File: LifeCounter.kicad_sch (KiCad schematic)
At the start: 22 parts, among them U1 MAX7221xWG, U2 CC56-12GWA, U3 CC56-12GWA, U4 74HC595

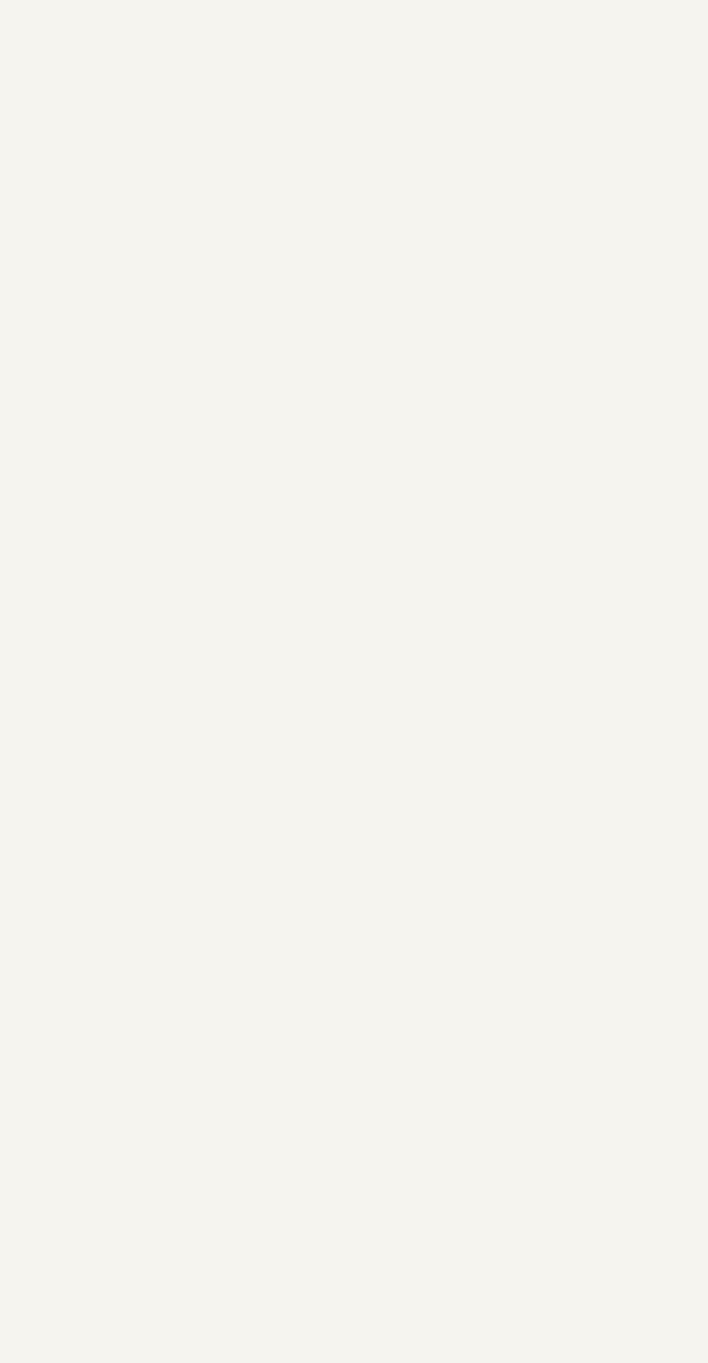
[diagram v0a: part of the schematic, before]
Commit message: Add encoders
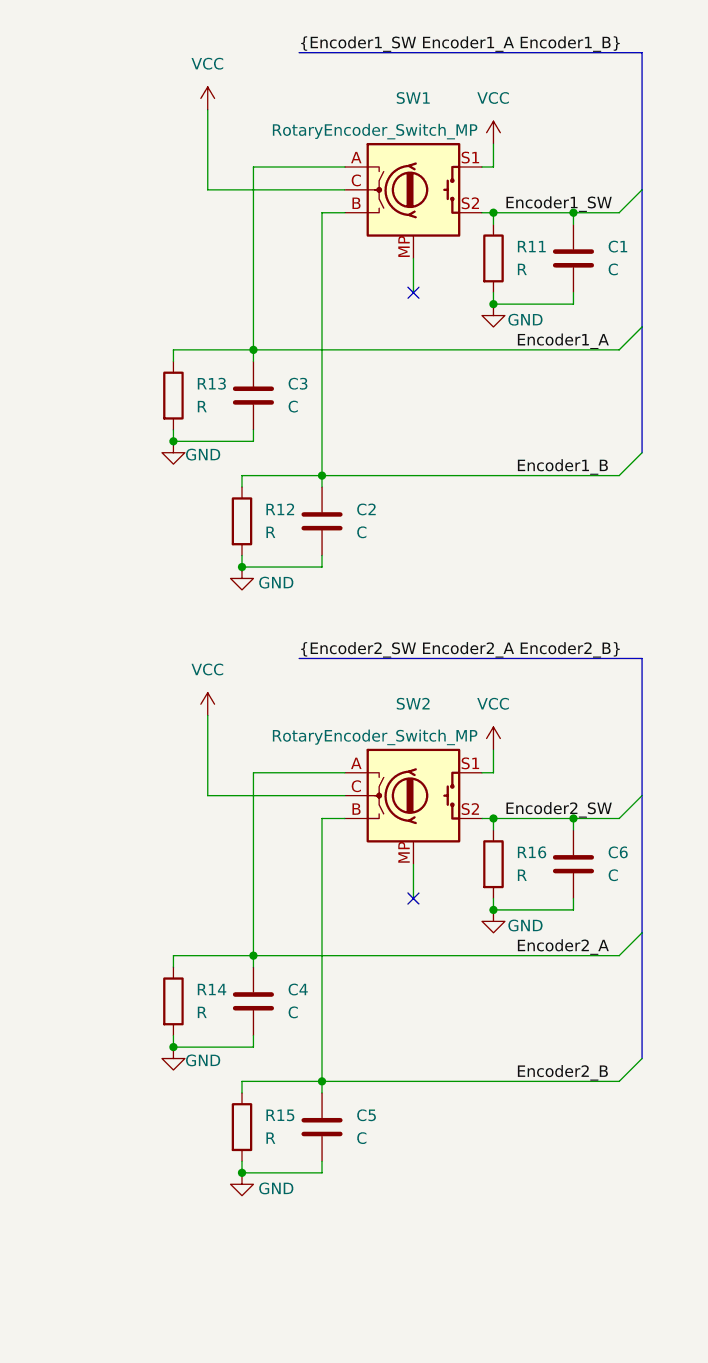
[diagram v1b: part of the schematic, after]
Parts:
- added C1, C2, C3, C4, C5, C6: C, symbol Device:C
- added R11, R12, R13, R14, R15, R16: R, symbol Device:R
- added SW1, SW2: RotaryEncoder_Switch_MP, symbol Device:RotaryEncoder_Switch_MP
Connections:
- net GND: now also C1.2, C2.2, C3.2, C4.2, C5.2, C6.2, R11.2, R12.2, R13.2, R14.2, R15.2, R16.2
- net VCC: now also SW1.C, SW1.S1, SW2.C, SW2.S1
- new net Encoder1_A: C3.1, R13.1, SW1.A
- new net Encoder1_B: C2.1, R12.1, SW1.B
- new net Encoder1_SW: C1.1, R11.1, SW1.S2
- new net Encoder2_A: C4.1, R14.1, SW2.A
- new net Encoder2_B: C5.1, R15.1, SW2.B
- new net Encoder2_SW: C6.1, R16.1, SW2.S2
- no-connect marks 2 -> 4

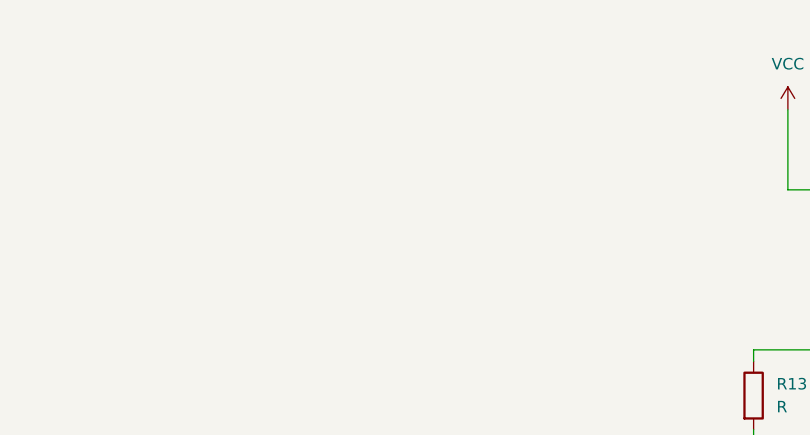
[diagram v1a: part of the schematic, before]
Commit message: Add buzzer
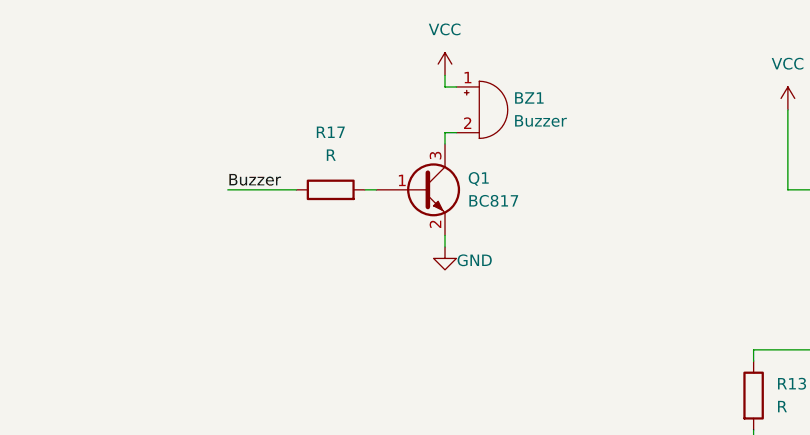
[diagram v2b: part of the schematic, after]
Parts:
- added BZ1: Buzzer, symbol Device:Buzzer
- added Q1: BC817, Package_TO_SOT_SMD:SOT-23, symbol Transistor_BJT:BC817
- added R17: R, symbol Device:R
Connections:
- net GND: now also Q1.2 (E)
- net VCC: now also BZ1.1 (+)
- new net: BZ1.2 (-), Q1.3 (C)
- new net: Q1.1 (B), R17.2
- new net Buzzer: R17.1

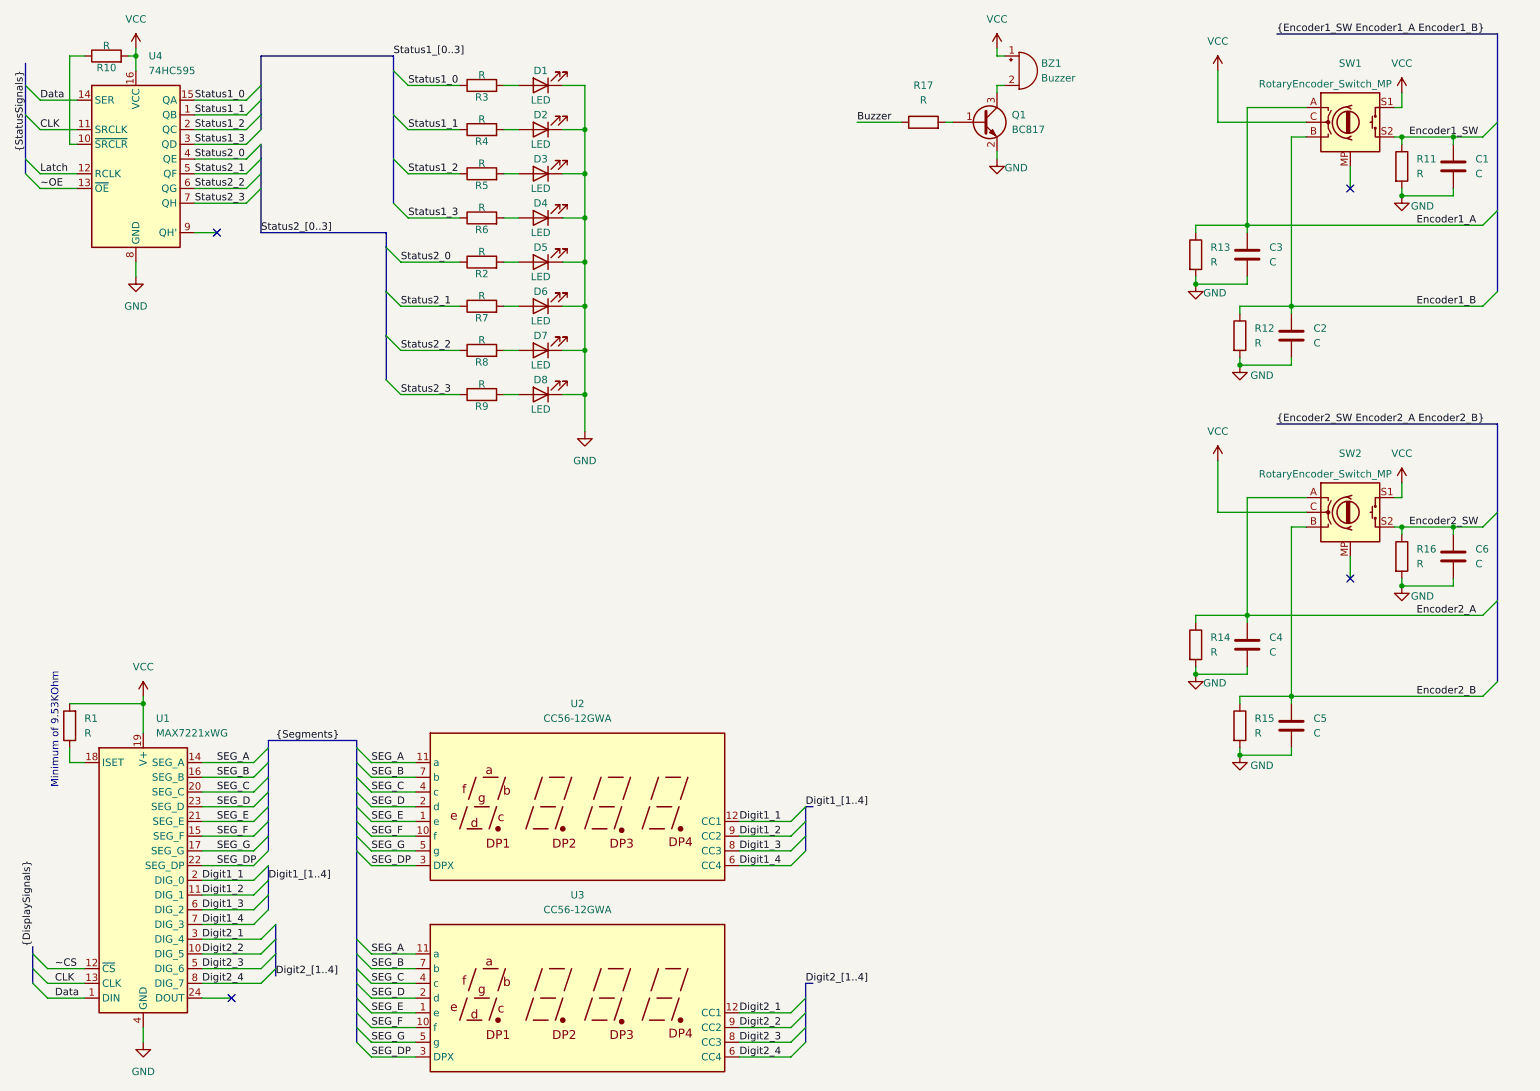
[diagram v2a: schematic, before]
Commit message: Split schematic into multiple sheets
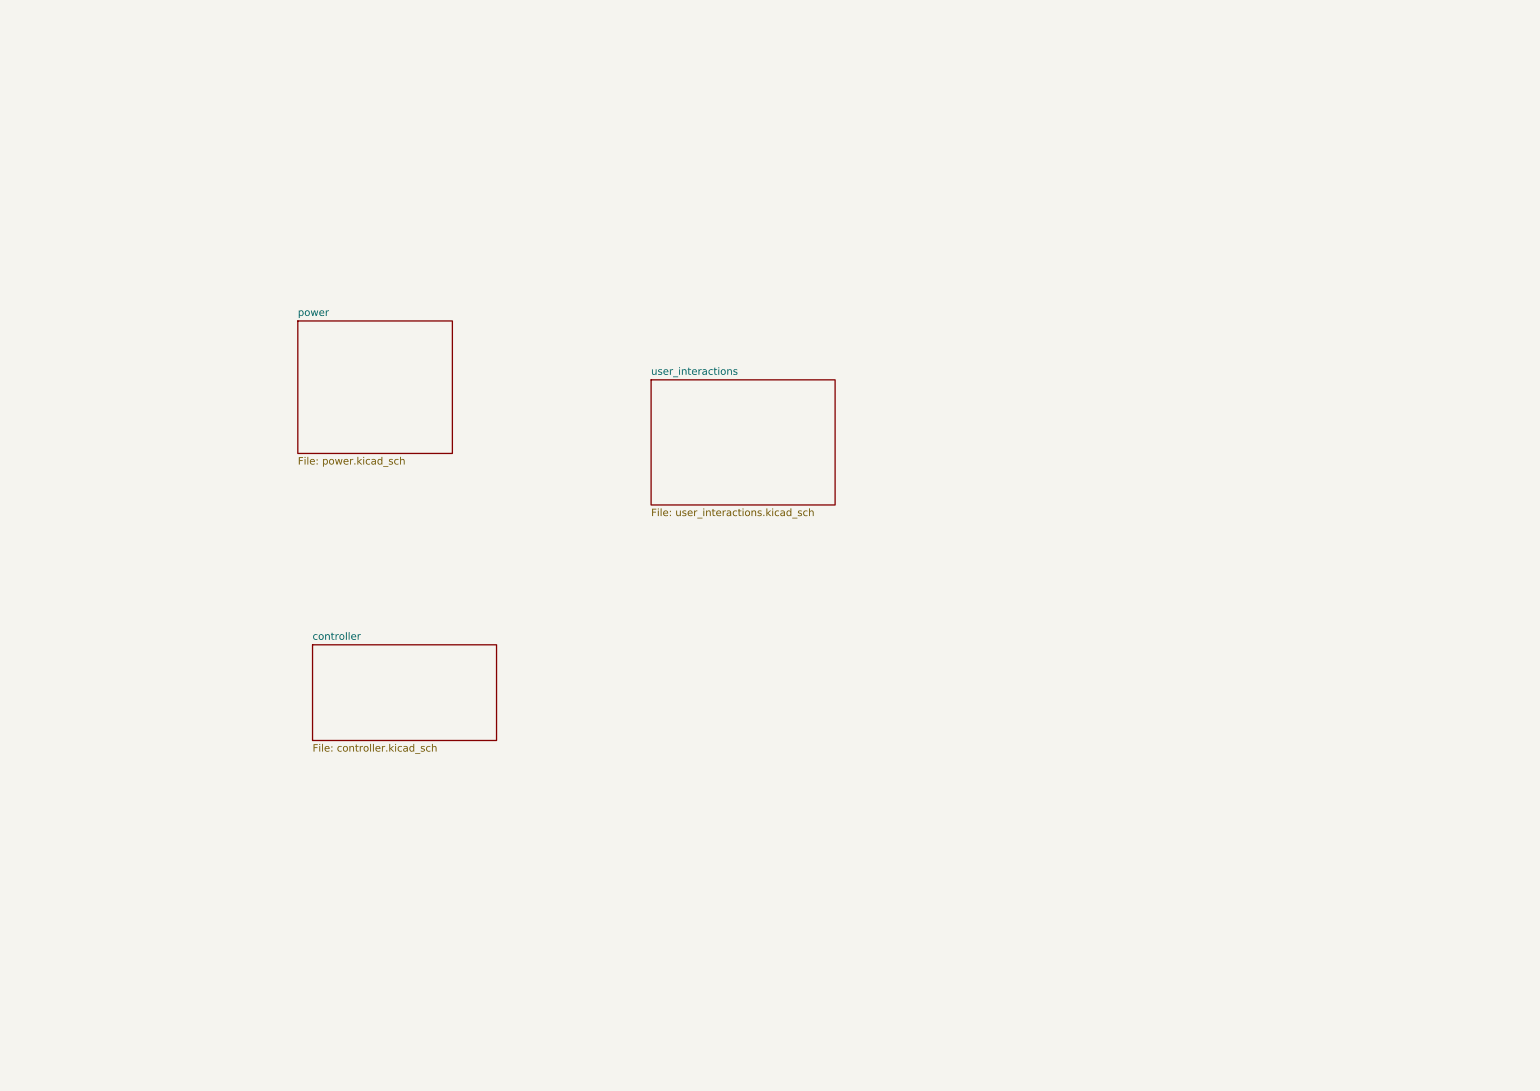
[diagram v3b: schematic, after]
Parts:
- removed BZ1: Buzzer, symbol Device:Buzzer
- removed C1, C2, C3, C4, C5, C6: C, symbol Device:C
- removed D1, D2, D3, D4, D5, D6, D7, D8: LED, symbol Device:LED
- removed Q1: BC817, Package_TO_SOT_SMD:SOT-23, symbol Transistor_BJT:BC817
- removed R1, R10, R11, R12, R13, R14, R15, R16, R17, R2, R3, R4, R5, R6, R7, R8, R9: R, symbol Device:R
- removed SW1, SW2: RotaryEncoder_Switch_MP, symbol Device:RotaryEncoder_Switch_MP
- removed U1: MAX7221xWG, Package_SO:SOIC-24W_7.5x15.4mm_P1.27mm, symbol Driver_LED:MAX7221xWG
- removed U2, U3: CC56-12GWA, Display_7Segment:CC56-12GWA, symbol Display_Character:CC56-12GWA
- removed U4: 74HC595, symbol 74xx:74HC595
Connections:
- no-connect marks 4 -> 0
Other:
- added sheet controller (controller.kicad_sch)
- added sheet power (power.kicad_sch)
- added sheet user_interactions (user_interactions.kicad_sch)
- note removed: "Minimum of 9.53KOhm"

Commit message: Power layout
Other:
- sheet user_interactions renamed io
- sheet io: file user_interactions.kicad_sch -> io.kicad_sch
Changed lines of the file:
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@@
 			(color 0 0 0 0.0000)
 		)
-		(property "Sheetname" "user_interactions"
+		(property "Sheetname" "io"
 			(at 137.16 75.4884 0)
 			(effects
@@
 			)
 		)
-		(property "Sheetfile" "user_interactions.kicad_sch"
+		(property "Sheetfile" "io.kicad_sch"
 			(at 137.16 98.3746 0)
 			(effects

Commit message: Controller selection
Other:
- sheet controller ports: added Buzzer, Display, Encoder1, Encoder2, FuelGage, POWER_ON, Status; removed none
- sheet io ports: added Buzzer, Display, Encoder1, Encoder2, Status; removed none
- sheet power ports: added FuelGage, POWER_ON; removed none
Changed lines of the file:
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@@
 		(members "Data" "CLK" "~OE" "Latch")
 	)
+	(bus
+		(pts
+			(xy 143.51 88.9) (xy 154.94 88.9)
+		)
+		(stroke
+			(width 0)
+			(type default)
+		)
+	)
+	(bus
+		(pts
+			(xy 143.51 91.44) (xy 154.94 91.44)
+		)
+		(stroke
+			(width 0)
+			(type default)
+		)
+	)
+	(wire
+		(pts
+			(xy 105.41 77.47) (xy 111.76 77.47)
+		)
+		(stroke
+			(width 0)
+			(type default)
+		)
+	)
+	(wire
+		(pts
+			(xy 143.51 82.55) (xy 154.94 82.55)
+		)
+		(stroke
+			(width 0)
+			(type default)
+		)
+	)
+	(bus
+		(pts
+			(xy 143.51 96.52) (xy 154.94 96.52)
+		)
+		(stroke
+			(width 0)
+			(type default)
+		)
+	)
+	(bus
+		(pts
+			(xy 105.41 81.28) (xy 111.76 81.28)
+		)
+		(stroke
+			(width 0)
+			(type default)
+		)
+	)
+	(bus
+		(pts
+			(xy 143.51 99.06) (xy 154.94 99.06)
+		)
+		(stroke
+			(width 0)
+			(type default)
+		)
+	)
 	(sheet
-		(at 78.74 121.92)
-		(size 31.75 16.51)
+		(at 111.76 73.66)
+		(size 31.75 33.02)
 		(fields_autoplaced yes)
 		(stroke
@@
 		)
 		(property "Sheetname" "controller"
-			(at 78.74 121.2084 0)
+			(at 111.76 72.9484 0)
 			(effects
 				(font
@@
 		)
 		(property "Sheetfile" "controller.kicad_sch"
-			(at 78.74 139.0146 0)
+			(at 111.76 107.2646 0)
 			(effects
 				(font
@@
 				)
 				(justify left top)
+			)
+		)
+		(pin "Buzzer" input
+			(at 143.51 82.55 0)
+			(effects
+				(font
+					(size 1.27 1.27)
+				)
+				(justify right)
+			)
+		)
+		(pin "POWER_ON" input
+			(at 111.76 77.47 180)
+			(effects
+				(font
+					(size 1.27 1.27)
+				)
+				(justify left)
+			)
+		)
+		(pin "Encoder1" input
+			(at 143.51 96.52 0)
+			(effects
+				(font
+					(size 1.27 1.27)
+				)
+				(justify right)
+			)
+		)
+		(pin "Encoder2" input
+			(at 143.51 99.06 0)
+			(effects
+				(font
+					(size 1.27 1.27)
+				)
+				(justify right)
+			)
+		)
+		(pin "Status" input
+			(at 143.51 88.9 0)
+			(effects
+				(font
+					(size 1.27 1.27)
+				)
+				(justify right)
+			)
+		)
+		(pin "Display" input
+			(at 143.51 91.44 0)
+			(effects
+				(font
+					(size 1.27 1.27)
+				)
+				(justify right)
+			)
+		)
+		(pin "FuelGage" input
+			(at 111.76 81.28 180)
+			(effects
+				(font
+					(size 1.27 1.27)
+				)
+				(justify left)
 			)
 		)
@@
 	)
 	(sheet
-		(at 137.16 76.2)
+		(at 154.94 80.01)
 		(size 31.75 21.59)
 		(fields_autoplaced yes)
@@
 		)
 		(property "Sheetname" "io"
-			(at 137.16 75.4884 0)
+			(at 154.94 79.2984 0)
 			(effects
 				(font
@@
 		)
 		(property "Sheetfile" "io.kicad_sch"
-			(at 137.16 98.3746 0)
+			(at 154.94 102.1846 0)
 			(effects
 				(font
@@
 				)
 				(justify left top)
+			)
+		)
+		(pin "Display" input
+			(at 154.94 91.44 180)
+			(effects
+				(font
+					(size 1.27 1.27)
+				)
+				(justify left)
+			)
+		)
+		(pin "Buzzer" input
+			(at 154.94 82.55 180)
+			(effects
+				(font
+					(size 1.27 1.27)
+				)
+				(justify left)
+			)
+		)
+		(pin "Encoder2" input
+			(at 154.94 99.06 180)
+			(effects
+				(font
+					(size 1.27 1.27)
+				)
+				(justify left)
+			)
+		)
+		(pin "Encoder1" input
+			(at 154.94 96.52 180)
+			(effects
+				(font
+					(size 1.27 1.27)
+				)
+				(justify left)
+			)
+		)
+		(pin "Status" input
+			(at 154.94 88.9 180)
+			(effects
+				(font
+					(size 1.27 1.27)
+				)
+				(justify left)
 			)
 		)
@@
 	)
 	(sheet
-		(at 76.2 66.04)
+		(at 78.74 72.39)
 		(size 26.67 22.86)
 		(fields_autoplaced yes)
@@
 		)
 		(property "Sheetname" "power"
-			(at 76.2 65.3284 0)
+			(at 78.74 71.6784 0)
 			(effects
 				(font
@@
 		)
 		(property "Sheetfile" "power.kicad_sch"
-			(at 76.2 89.4846 0)
+			(at 78.74 95.8346 0)
 			(effects
 				(font
@@
 			)
 		)
+		(pin "POWER_ON" input
+			(at 105.41 77.47 0)
+			(effects
+				(font
+					(size 1.27 1.27)
+				)
+				(justify right)
+			)
+		)
+		(pin "FuelGage" input
+			(at 105.41 81.28 0)
+			(effects
+				(font
+					(size 1.27 1.27)
+				)
+				(justify right)
+			)
+		)
